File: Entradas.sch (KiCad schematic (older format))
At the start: 22 parts, among them U9 SI8380P-IU

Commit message: Esq + PCB + Bom terminados
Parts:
- C9: DigikeyPage (none) -> https://www.digikey.com/products/en?keywords=CL31B104KBCNNN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; Manf (none) -> Samsung
- JE1, JE2, JE3: value TB_1X2 -> TB_1X2-PonchoPLC-rescue; Desc (none) -> Terminal Block - Header, Male Pins, Shrouded -5mm -2 pos; Digikey# (none) -> A98062-ND; DigikeyPage (none) -> https://www.digikey.com/products/en?keywords=A98062-ND%20; Manf (none) -> Weco
- JE4: value TB_1X3 -> TB_1X3-PonchoPLC-rescue; Desc (none) -> Terminal Block - Header, Male Pins, Shrouded -5mm -3 pos; Digikey# (none) -> A98063-ND; DigikeyPage (none) -> https://www.digikey.com/products/en?keywords=A98063-ND; Manf (none) -> Weco
- R17, R19, R21, R23, R25, R27, R29, R31: Digikey# CR0805-JW-622ELFTR-ND -> CR0805-JW-622ELFTR-ND; DigikeyPage (none) -> https://www.digikey.com/products/en?keywords=CR0805-JW-622E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; Manf CR0805-JW-622ELFTR-ND -> Bourns
- R18, R20, R22, R24, R26, R28, R30, R32: DigikeyPage (none) -> https://www.digikey.com/products/en?keywords=CR0805-JW-272E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; Manf (none) -> Bourns
- U9: Digikey# 336-3618-5-ND -> 336-3618-5-ND; DigikeyPage (none) -> https://www.digikey.com/products/en?keywords=336-3618-5-ND%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; Manf (none) -> Silabs

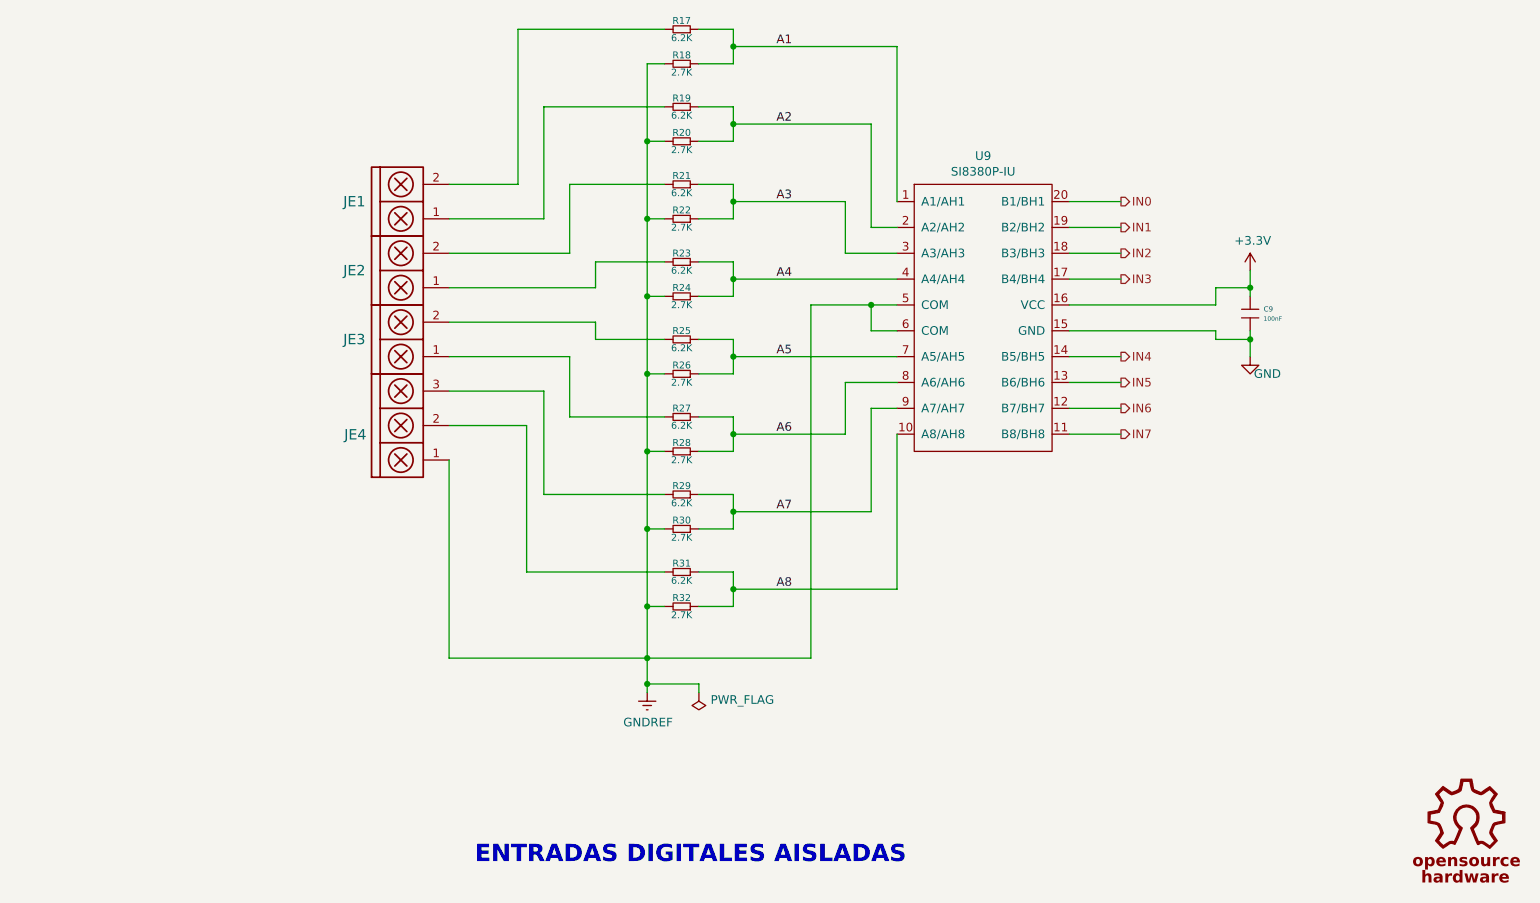
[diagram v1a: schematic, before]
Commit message: Agregado Leds Entradas
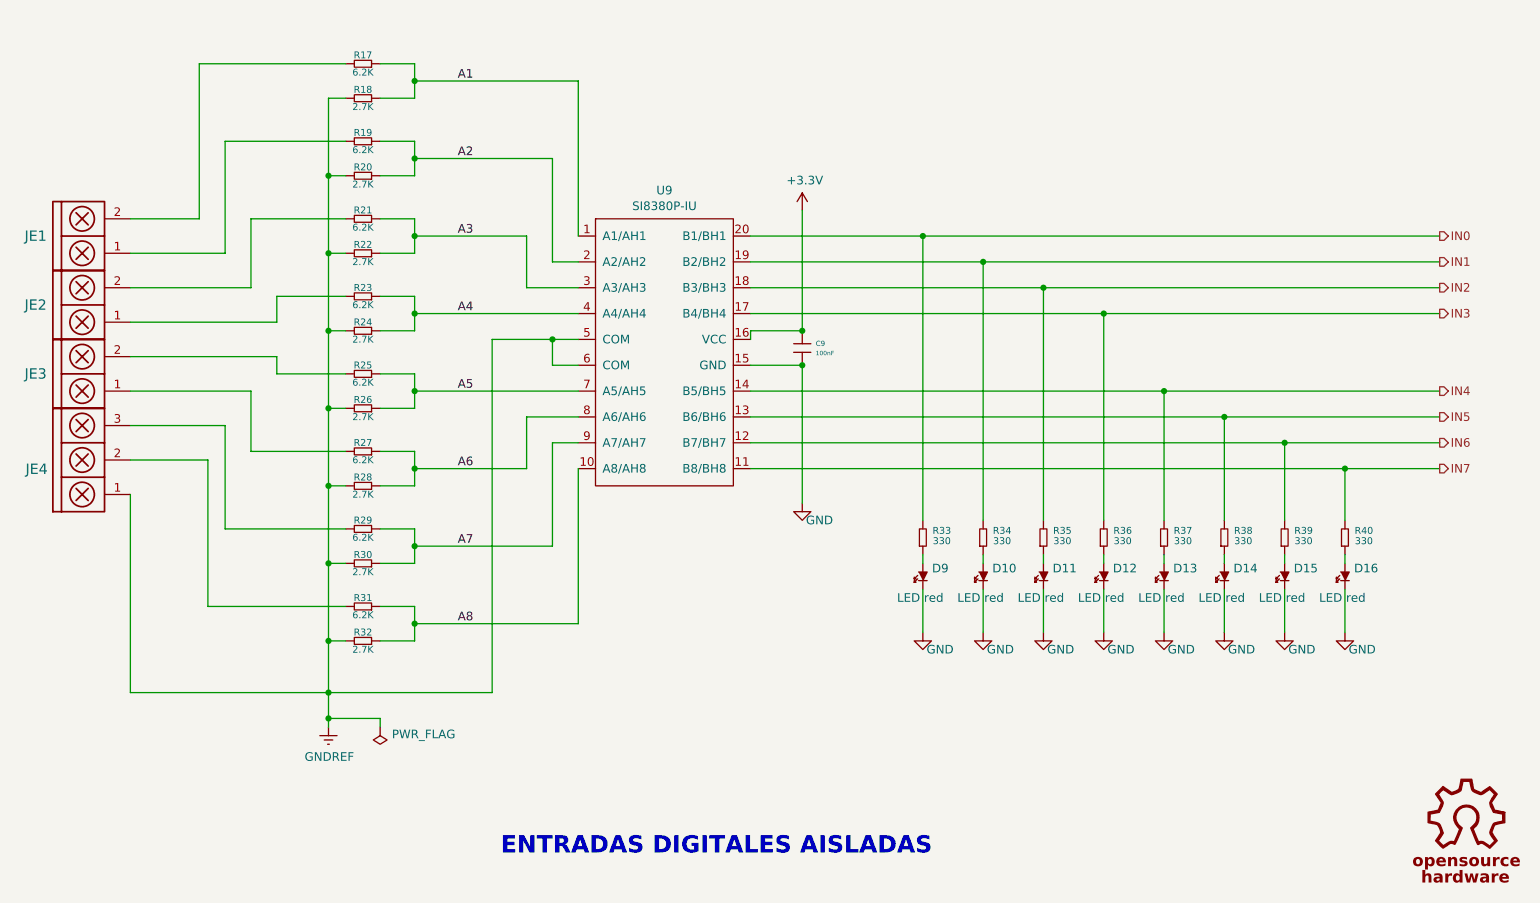
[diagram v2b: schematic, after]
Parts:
- added D10, D11, D12, D13, D14, D15, D16, D9: LED red, LED_SMD:LED_0805_2012Metric, symbol Poncho-PLC7-rescue:LED
- added R33, R34, R35, R36, R37, R38, R39, R40: 330, Resistor_SMD:R_0805_2012Metric, symbol Poncho-PLC7-rescue:R
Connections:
- net GND: now also D10.2 (K), D11.2 (K), D12.2 (K), D13.2 (K), D14.2 (K), D15.2 (K), D16.2 (K), D9.2 (K)
- net IN0: now also R33.2
- net IN1: now also R34.2
- net IN2: now also R35.2
- net IN3: now also R36.2
- net IN4: now also R37.2
- net IN5: now also R38.2
- net IN6: now also R39.2
- net IN7: now also R40.2
- new net: D9.1 (A), R33.1
- new net: D10.1 (A), R34.1
- new net: D11.1 (A), R35.1
- new net: D12.1 (A), R36.1
- new net: D13.1 (A), R37.1
- new net: D14.1 (A), R38.1
- new net: D15.1 (A), R39.1
- new net: D16.1 (A), R40.1
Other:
- moved on the sheet: C9, JE1, JE2, JE3, JE4, R17, R18, R19, R20, R21, R22, R23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
